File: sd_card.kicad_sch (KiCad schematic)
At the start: 9 parts, among them J8 uSD card

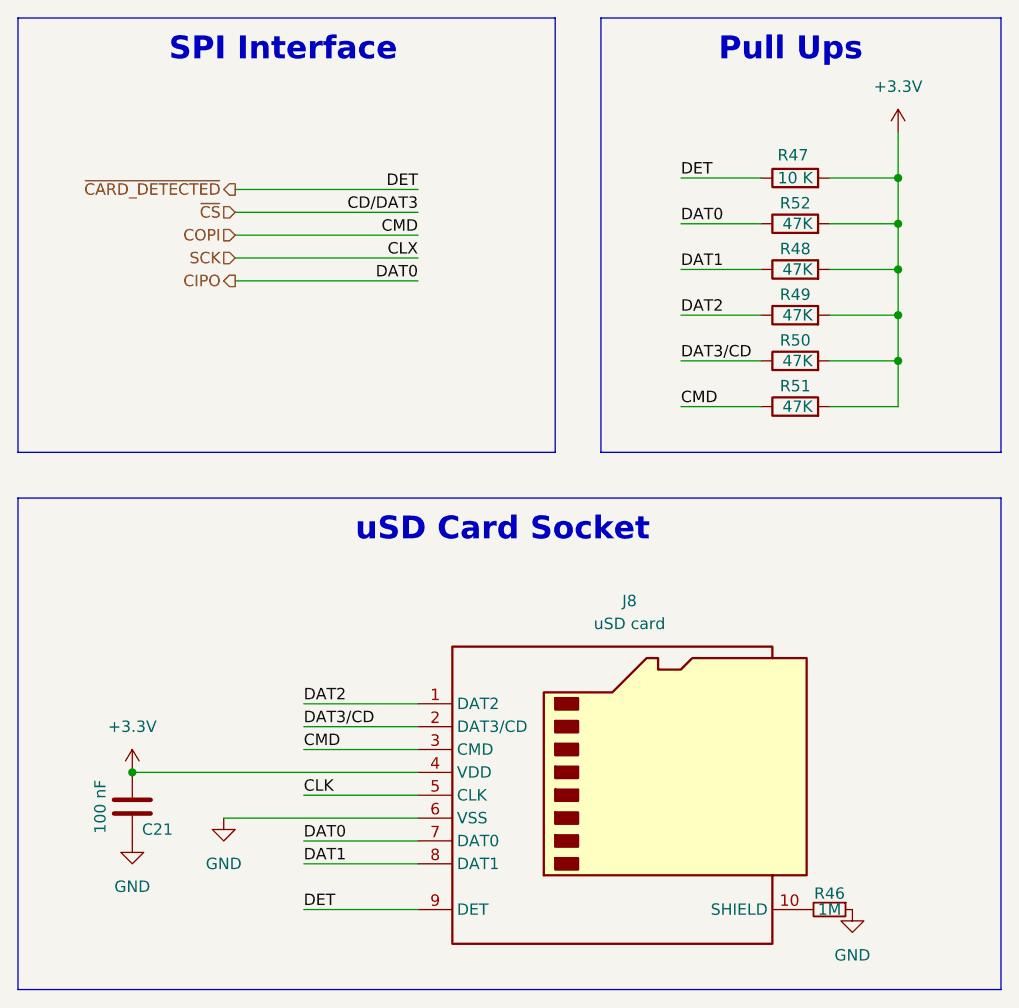
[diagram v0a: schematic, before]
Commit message: Schematics: Add accelerometer, drop VBAT sensing
Adding a cheap accelerometer to the boards, sacraficing the VBAT input
to make room for the /CS pin.
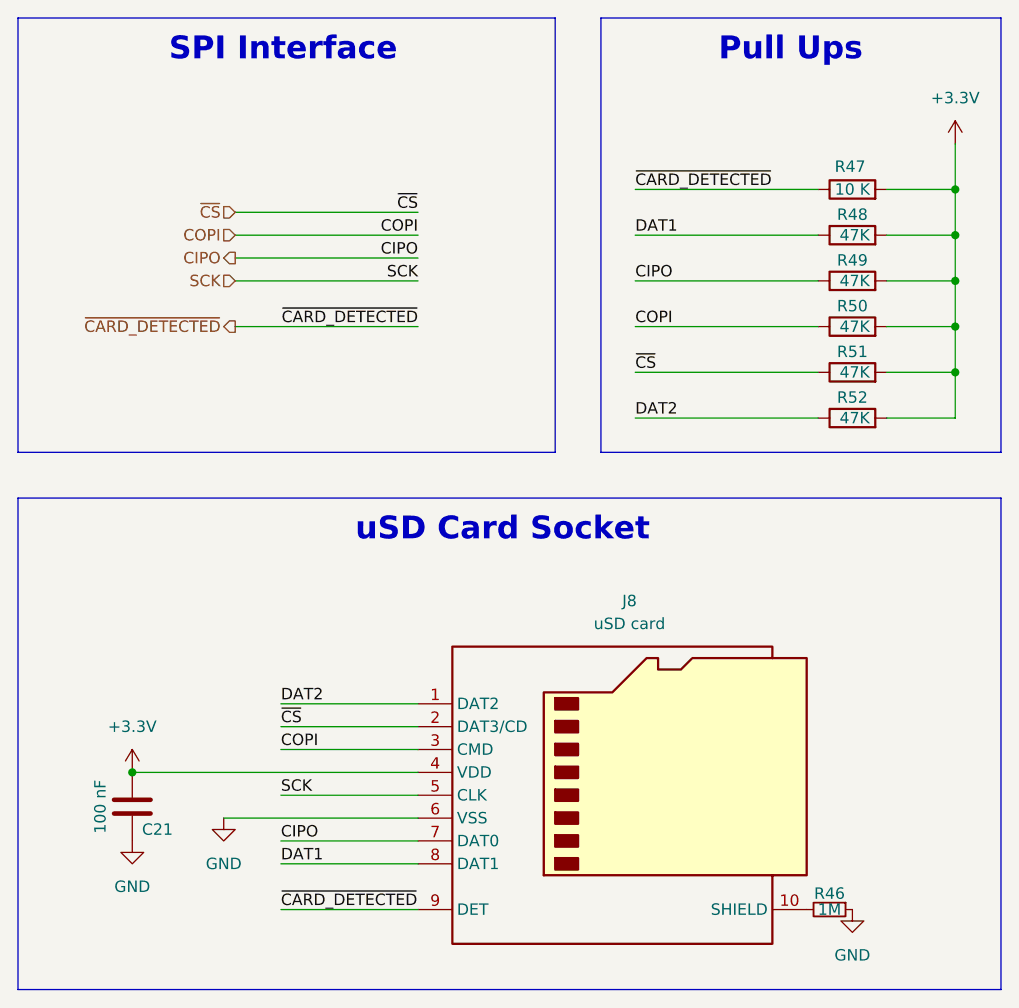
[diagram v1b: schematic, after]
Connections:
- net CLK is gone; now on net SCK: J8.5 (CLK)
- net CIPO: now also R49.1; no longer R52.1
- net COPI: now also R50.1; no longer R51.1
- net DAT2: now also R52.1; no longer R49.1
- net ~{CS}: now also J8.2 (DAT3/CD), R51.1
- removed net DAT3/CD: J8.2 (DAT3/CD), R50.1
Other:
- moved on the sheet: R47, R48, R49, R50, R51, R52
